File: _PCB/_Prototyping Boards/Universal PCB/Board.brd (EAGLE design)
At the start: 60 x 40 mm, 6 parts

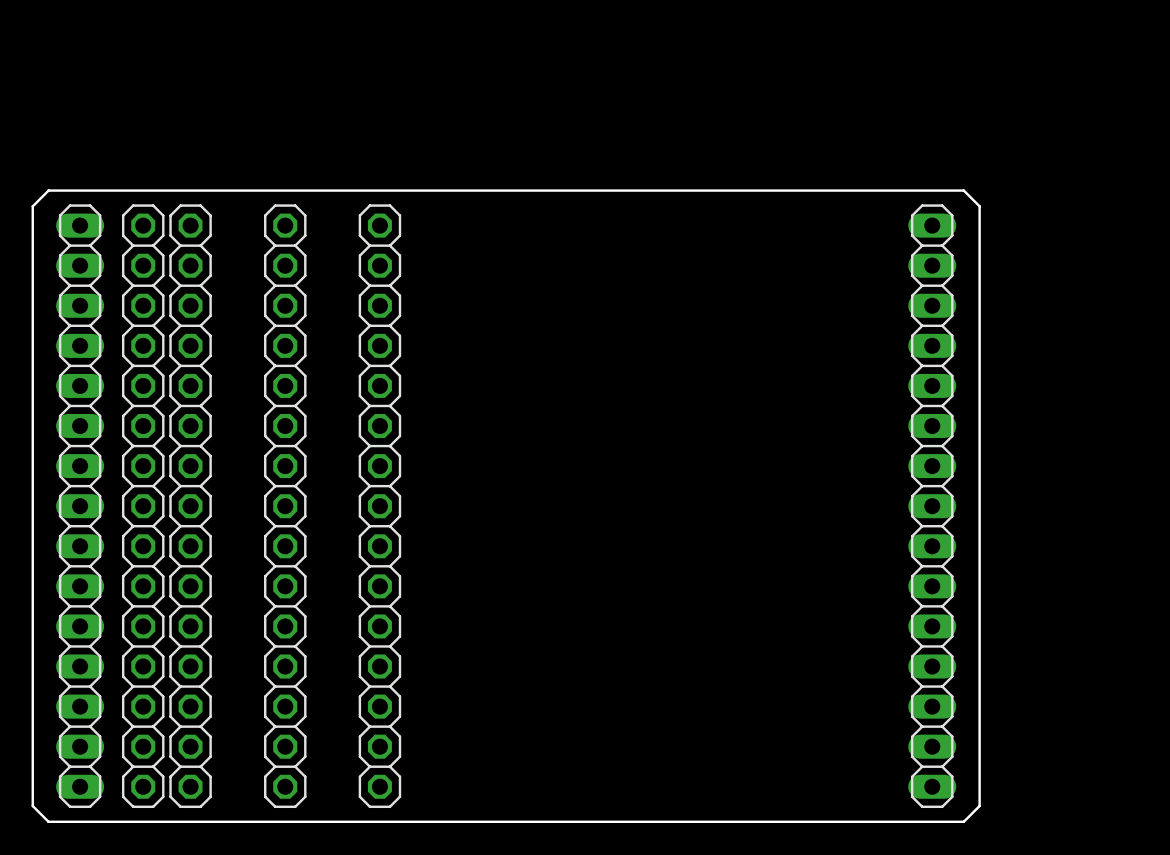
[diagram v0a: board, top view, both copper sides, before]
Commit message: LoRa sensor + universal PCB
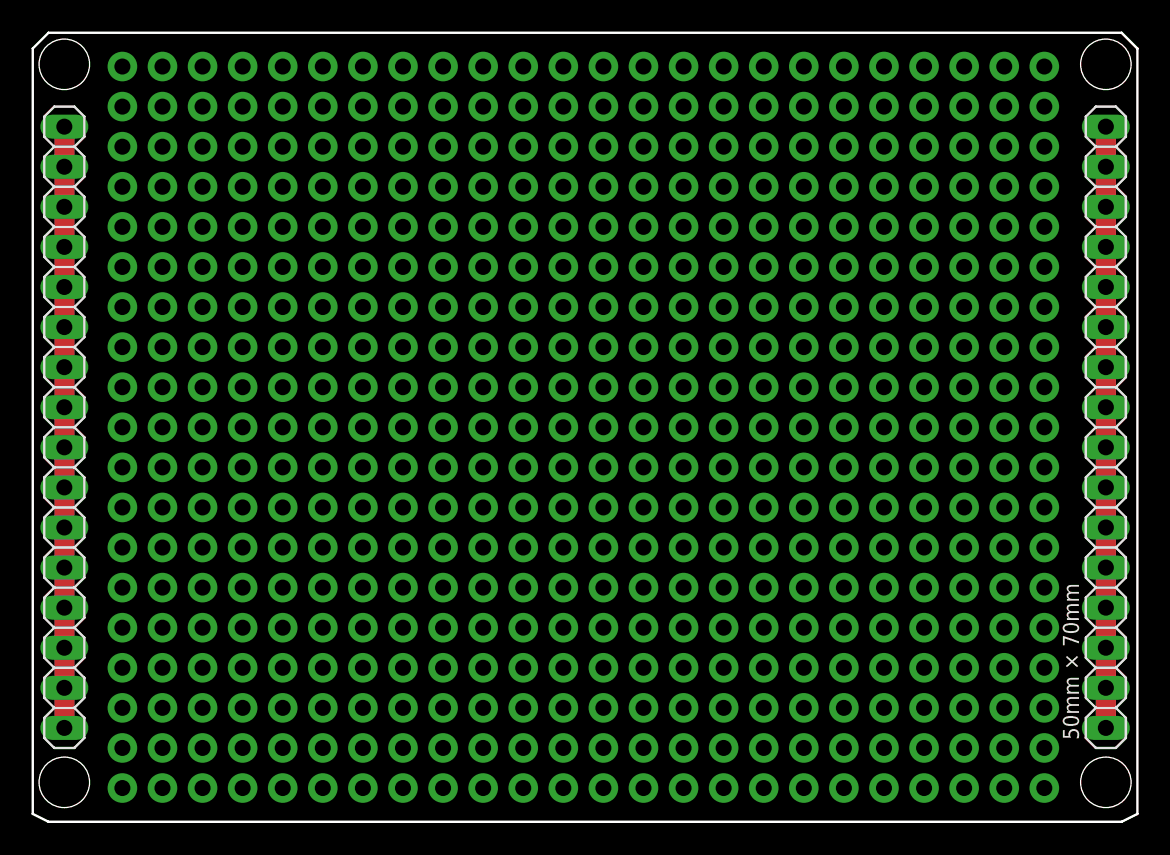
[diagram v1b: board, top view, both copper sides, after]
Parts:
- removed JP1, JP2: (no value), pinhead_v2:1X15/OCT
- removed JP5, JP6: (no value), pinhead_v2:1X15
- added J10, J11, J12, J13, J14, J15, J16, J17, J18, J19, J2, J20, J21, J22, J23, J24, J25, J3, J4, J5, J6, J7, J8, J9: (no value), SparkFun-Connectors:1X19_NO_SILK
- JP3, JP4: device pinhead_v2:1X15/OCT -> pinhead_v2:1X16
- moved JP3 61.2 mm to (68.0, 25.0)
- moved JP4 20.6 mm to (2.00, 25.0)
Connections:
- new net SIDE1: JP4.1, JP4.10, JP4.11, JP4.12, JP4.13, JP4.14, JP4.15, JP4.16, JP4.2, JP4.3, JP4.4, JP4.5, JP4.6, JP4.7, JP4.8, JP4.9
- new net SIDE2: JP3.1, JP3.10, JP3.11, JP3.12, JP3.13, JP3.14, JP3.15, JP3.16, JP3.2, JP3.3, JP3.4, JP3.5, JP3.6, JP3.7, JP3.8, JP3.9
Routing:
- net S$4: track 0.00 -> 38.0 mm
- net S$3: track 0.00 -> 38.0 mm
- net S$2: track 0.00 -> 38.0 mm
- net S$1: track 0.00 -> 38.0 mm
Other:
- board size 60 x 40 mm -> 70 x 50 mm
- board text added: "50mm × 70mm"
